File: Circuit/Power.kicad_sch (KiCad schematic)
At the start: 8 parts, among them J9 Conn_01x05_Pin

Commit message: Output job, Revision Box and reorganise
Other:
- company: Harry and Yuki - EEE3 Instrumentation -> Harry Hill and Yuki Hoshino
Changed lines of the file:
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@@
 	(title_block
 		(title "Power Supply")
-		(date "2026-03-02")
+		(date "2026-05-02")
 		(rev "1.0")
-		(company "Harry and Yuki - EEE3 Instrumentation")
+		(company "Harry Hill and Yuki Hoshino")
+		(comment 1 "LCR Meter")
 	)
 	(text "18V \n12V \n3.3V \nGND \n-18V\n"

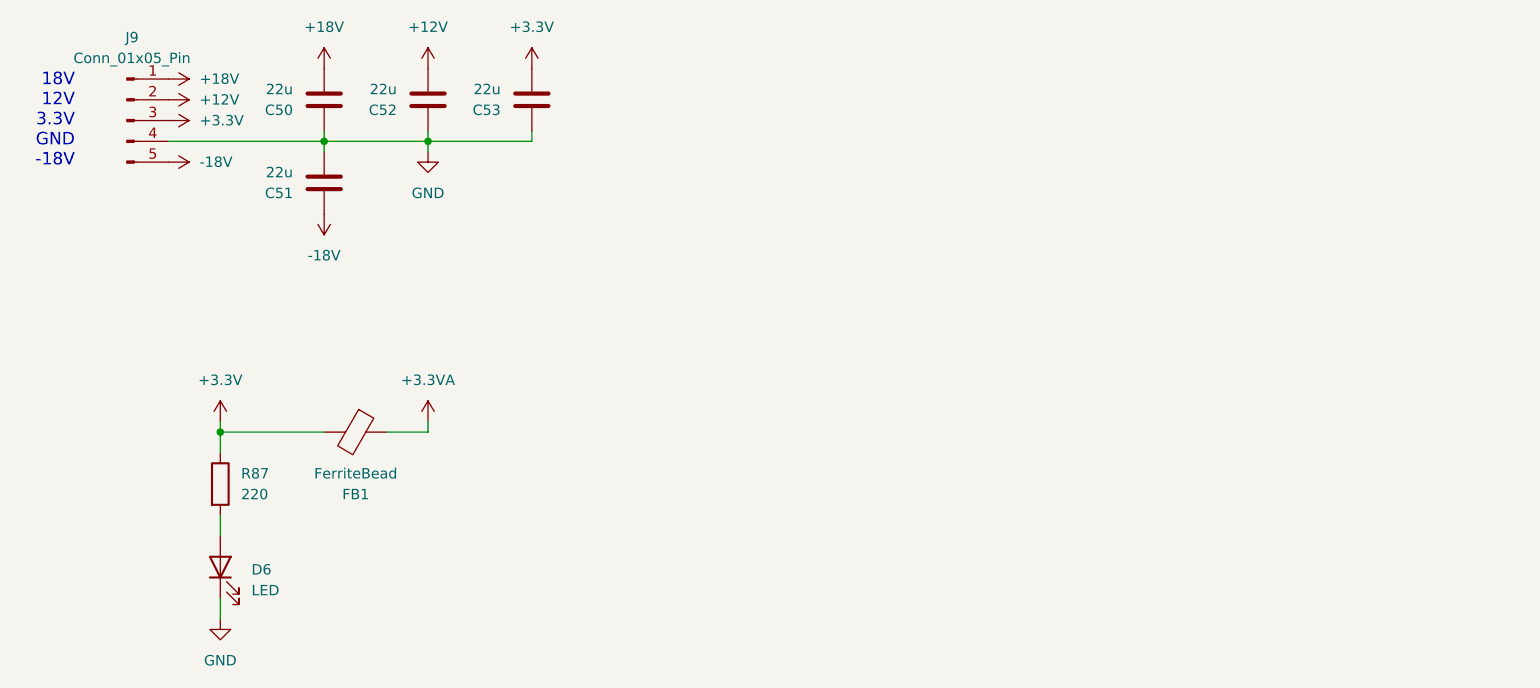
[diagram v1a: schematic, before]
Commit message: Input Protection Second Attempt
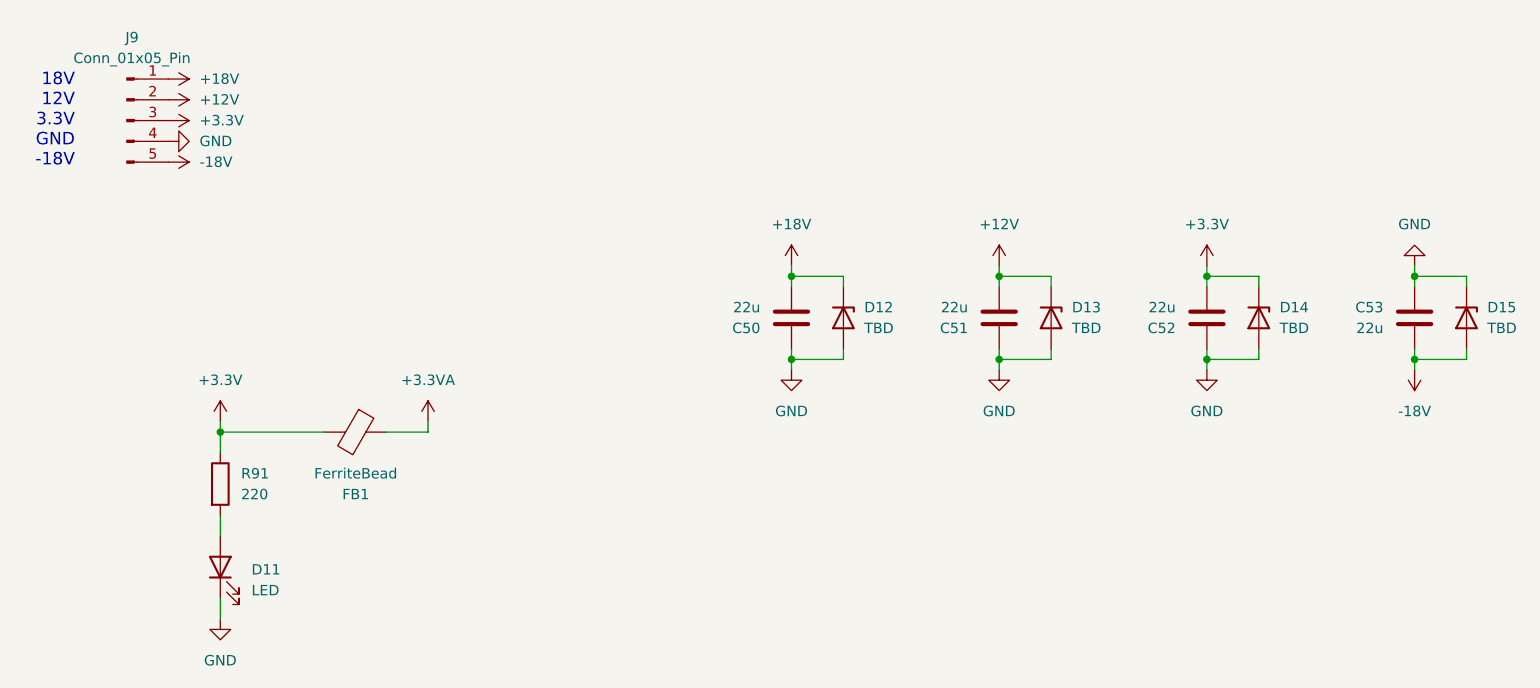
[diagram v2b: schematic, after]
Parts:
- removed C51: 22u, Capacitor_SMD:C_1210_3225Metric, symbol Device:C
- added C53: 22u, Capacitor_SMD:C_1210_3225Metric, symbol Device:C
- added D12, D13, D14, D15: TBD, Diode_SMD:D_SMA, symbol Device:D_Zener
- renumbered C52 to C51, C53 to C52, D6 to D11, R87 to R91
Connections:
- net +12V: now also D13.1 (K)
- net +18V: now also D12.1 (K)
- net +3.3V: now also D14.1 (K)
- net -18V: now also C53.1, D15.2 (A)
- net GND: now also C53.2, D12.2 (A), D13.2 (A), D14.2 (A), D15.1 (K)
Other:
- moved on the sheet: C50, C51, C52

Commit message: New Resistor Selection Circuit
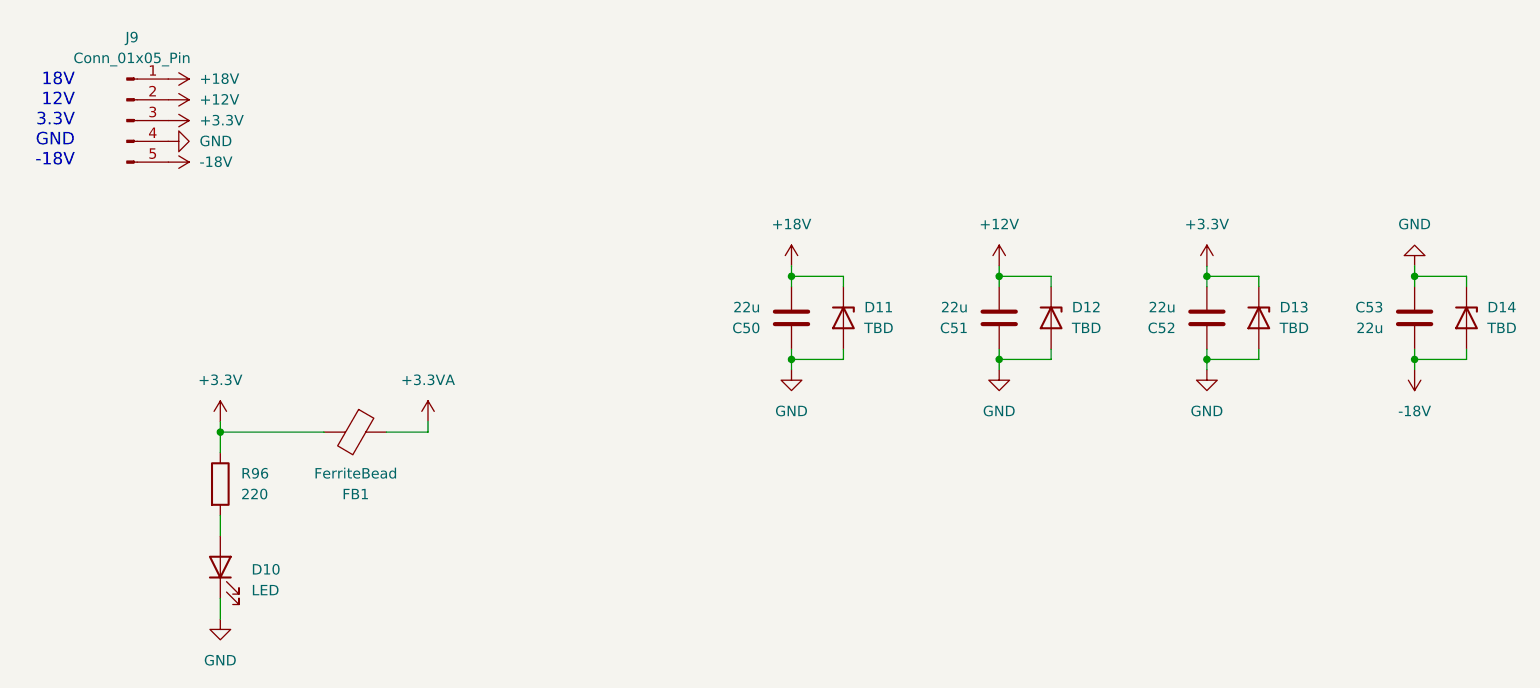
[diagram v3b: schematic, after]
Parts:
- renumbered D11 to D10, D12 to D11, D13 to D12, D14 to D13, D15 to D14, R91 to R96
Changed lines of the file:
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@@
 		(dnp no)
 		(fields_autoplaced yes)
-		(property "Reference" "R91"
+		(property "Reference" "R96"
 			(at 123.19 101.5999 0)
 			(effects
@@
 			(project "Main Board"
 				(path "/20aae4b7-3fb8-4924-82e8-1e7a29a313f8/19c51356-5fe8-4a9f-9623-d1f705fed6f9"
-					(reference "R91")
+					(reference "R96")
 					(unit 1)
 				)
@@
 		(dnp no)
 		(fields_autoplaced yes)
-		(property "Reference" "#PWR0146"
+		(property "Reference" "#PWR0145"
 			(at 266.7 69.85 0)
 			(effects
@@
 			(project "Main Board"
 				(path "/20aae4b7-3fb8-4924-82e8-1e7a29a313f8/19c51356-5fe8-4a9f-9623-d1f705fed6f9"
-					(reference "#PWR0146")
+					(reference "#PWR0145")
 					(unit 1)
 				)
@@
 		(dnp no)
 		(fields_autoplaced yes)
-		(property "Reference" "D15"
+		(property "Reference" "D14"
 			(at 275.59 81.2799 90)
 			(effects
@@
 			(project "Main Board"
 				(path "/20aae4b7-3fb8-4924-82e8-1e7a29a313f8/19c51356-5fe8-4a9f-9623-d1f705fed6f9"
-					(reference "D15")
+					(reference "D14")
 					(unit 1)
 				)
@@
 		(dnp no)
 		(fields_autoplaced yes)
-		(property "Reference" "#PWR0137"
+		(property "Reference" "#PWR0136"
 			(at 120.65 99.06 0)
 			(effects
@@
 			(project "Main Board"
 				(path "/20aae4b7-3fb8-4924-82e8-1e7a29a313f8/19c51356-5fe8-4a9f-9623-d1f705fed6f9"
-					(reference "#PWR0137")
+					(reference "#PWR0136")
 					(unit 1)
 				)
@@
 		(dnp no)
 		(fields_autoplaced yes)
-		(property "Reference" "#PWR0147"
+		(property "Reference" "#PWR0146"
 			(at 266.7 85.09 0)
 			(effects
@@
 			(project "Main Board"
 				(path "/20aae4b7-3fb8-4924-82e8-1e7a29a313f8/19c51356-5fe8-4a9f-9623-d1f705fed6f9"
-					(reference "#PWR0147")
+					(reference "#PWR0146")
 					(unit 1)
 				)
@@
 		(dnp no)
 		(fields_autoplaced yes)
-		(property "Reference" "#PWR0132"
+		(property "Reference" "#PWR0131"
 			(at 110.49 53.34 0)
 			(effects
@@
 			(project "Main Board"
 				(path "/20aae4b7-3fb8-4924-82e8-1e7a29a313f8/19c51356-5fe8-4a9f-9623-d1f705fed6f9"
-					(reference "#PWR0132")
+					(reference "#PWR0131")
 					(unit 1)
 				)
@@
 		(dnp no)
 		(fields_autoplaced yes)
-		(property "Reference" "#PWR0139"
+		(property "Reference" "#PWR0138"
 			(at 146.05 99.06 0)
 			(effects
@@
 			(project ""
 				(path "/20aae4b7-3fb8-4924-82e8-1e7a29a313f8/19c51356-5fe8-4a9f-9623-d1f705fed6f9"
-					(reference "#PWR0139")
+					(reference "#PWR0138")
 					(unit 1)
 				)
@@
 		(dnp no)
 		(fields_autoplaced yes)
-		(property "Reference" "#PWR0136"
+		(property "Reference" "#PWR0135"
 			(at 110.49 63.5 0)
 			(effects
@@
 			(project "Main Board"
 				(path "/20aae4b7-3fb8-4924-82e8-1e7a29a313f8/19c51356-5fe8-4a9f-9623-d1f705fed6f9"
-					(reference "#PWR0136")
+					(reference "#PWR0135")
 					(unit 1)
 				)
@@
 		(dnp no)
 		(fields_autoplaced yes)
-		(property "Reference" "#PWR0144"
+		(property "Reference" "#PWR0143"
 			(at 241.3 80.01 0)
 			(effects
@@
 			(project "Main Board"
 				(path "/20aae4b7-3fb8-4924-82e8-1e7a29a313f8/19c51356-5fe8-4a9f-9623-d1f705fed6f9"
-					(reference "#PWR0144")
+					(reference "#PWR0143")
 					(unit 1)
 				)
@@
 		(dnp no)
 		(fields_autoplaced yes)
-		(property "Reference" "#PWR0140"
+		(property "Reference" "#PWR0139"
 			(at 190.5 80.01 0)
 			(effects
@@
 			(project "Main Board"
 				(path "/20aae4b7-3fb8-4924-82e8-1e7a29a313f8/19c51356-5fe8-4a9f-9623-d1f705fed6f9"
-					(reference "#PWR0140")
+					(reference "#PWR0139")
 					(unit 1)
 				)
@@
 		(dnp no)
 		(fields_autoplaced yes)
-		(property "Reference" "#PWR0135"
+		(property "Reference" "#PWR0134"
 			(at 120.65 60.96 0)
 			(effects
@@
 			(project ""
 				(path "/20aae4b7-3fb8-4924-82e8-1e7a29a313f8/19c51356-5fe8-4a9f-9623-d1f705fed6f9"
-					(reference "#PWR0135")
+					(reference "#PWR0134")
 					(unit 1)
 				)
@@
 		(dnp no)
 		(fields_autoplaced yes)
-		(property "Reference" "#PWR0145"
+		(property "Reference" "#PWR0144"
 			(at 241.3 95.25 0)
 			(effects
@@
 			(project "Main Board"
 				(path "/20aae4b7-3fb8-4924-82e8-1e7a29a313f8/19c51356-5fe8-4a9f-9623-d1f705fed6f9"
-					(reference "#PWR0145")
+					(reference "#PWR0144")
 					(unit 1)
 				)
@@
 		(dnp no)
 		(fields_autoplaced yes)
-		(property "Reference" "#PWR0138"
+		(property "Reference" "#PWR0137"
 			(at 120.65 125.73 0)
 			(effects
@@
 			(project "Main Board"
 				(path "/20aae4b7-3fb8-4924-82e8-1e7a29a313f8/19c51356-5fe8-4a9f-9623-d1f705fed6f9"
-					(reference "#PWR0138")
+					(reference "#PWR0137")
 					(unit 1)
 				)
@@
 		(dnp no)
 		(fields_autoplaced yes)
-		(property "Reference" "#PWR0143"
+		(property "Reference" "#PWR0142"
 			(at 215.9 95.25 0)
 			(effects
@@
 			(project "Main Board"
 				(path "/20aae4b7-3fb8-4924-82e8-1e7a29a313f8/19c51356-5fe8-4a9f-9623-d1f705fed6f9"
-					(reference "#PWR0143")
+					(reference "#PWR0142")
 					(unit 1)
 				)
@@
 		(dnp no)
 		(fields_autoplaced yes)
-		(property "Reference" "D11"
+		(property "Reference" "D10"
 			(at 124.46 113.3474 90)
 			(effects
@@
 			(project ""
 				(path "/20aae4b7-3fb8-4924-82e8-1e7a29a313f8/19c51356-5fe8-4a9f-9623-d1f705fed6f9"
-					(reference "D11")
+					(reference "D10")
 					(unit 1)
 				)
@@
 		(dnp no)
 		(fields_autoplaced yes)
-		(property "Reference" "#PWR0141"
+		(property "Reference" "#PWR0140"
 			(at 190.5 95.25 0)
 			(effects
@@
 			(project "Main Board"
 				(path "/20aae4b7-3fb8-4924-82e8-1e7a29a313f8/19c51356-5fe8-4a9f-9623-d1f705fed6f9"
-					(reference "#PWR0141")
+					(reference "#PWR0140")
 					(unit 1)
 				)
@@
 		(dnp no)
 		(fields_autoplaced yes)
-		(property "Reference" "D12"
+		(property "Reference" "D11"
 			(at 199.39 81.2799 90)
 			(effects
@@
 			(project ""
 				(path "/20aae4b7-3fb8-4924-82e8-1e7a29a313f8/19c51356-5fe8-4a9f-9623-d1f705fed6f9"
-					(reference "D12")
+					(reference "D11")
 					(unit 1)
 				)
@@
 		(dnp no)
 		(fields_autoplaced yes)
-		(property "Reference" "#PWR0134"
+		(property "Reference" "#PWR0133"
 			(at 110.49 58.42 0)
 			(effects
@@
 			(project "Main Board"
 				(path "/20aae4b7-3fb8-4924-82e8-1e7a29a313f8/19c51356-5fe8-4a9f-9623-d1f705fed6f9"
-					(reference "#PWR0134")
+					(reference "#PWR0133")
 					(unit 1)
 				)
@@
 		(dnp no)
 		(fields_autoplaced yes)
-		(property "Reference" "D14"
+		(property "Reference" "D13"
 			(at 250.19 81.2799 90)
 			(effects
@@
 			(project "Main Board"
 				(path "/20aae4b7-3fb8-4924-82e8-1e7a29a313f8/19c51356-5fe8-4a9f-9623-d1f705fed6f9"
-					(reference "D14")
+					(reference "D13")
 					(unit 1)
 				)
@@
 		(dnp no)
 		(fields_autoplaced yes)
-		(property "Reference" "#PWR0133"
+		(property "Reference" "#PWR0132"
 			(at 110.49 55.88 0)
 			(effects
@@
 			(project "Main Board"
 				(path "/20aae4b7-3fb8-4924-82e8-1e7a29a313f8/19c51356-5fe8-4a9f-9623-d1f705fed6f9"
-					(reference "#PWR0133")
+					(reference "#PWR0132")
 					(unit 1)
 				)
@@
 		(dnp no)
 		(fields_autoplaced yes)
-		(property "Reference" "D13"
+		(property "Reference" "D12"
 			(at 224.79 81.2799 90)
 			(effects
@@
 			(project "Main Board"
 				(path "/20aae4b7-3fb8-4924-82e8-1e7a29a313f8/19c51356-5fe8-4a9f-9623-d1f705fed6f9"
-					(reference "D13")
+					(reference "D12")
 					(unit 1)
 				)
@@
 		(dnp no)
 		(fields_autoplaced yes)
-		(property "Reference" "#PWR0142"
+		(property "Reference" "#PWR0141"
 			(at 215.9 80.01 0)
 			(effects
@@
 			(project "Main Board"
 				(path "/20aae4b7-3fb8-4924-82e8-1e7a29a313f8/19c51356-5fe8-4a9f-9623-d1f705fed6f9"
-					(reference "#PWR0142")
-					(unit 1)
-				)
+					(reference "#PWR0141")
+					(unit 1)
+				)
